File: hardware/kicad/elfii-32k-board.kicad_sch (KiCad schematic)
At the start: 14 parts, among them J1 ELFII_P3_86, SW1 RAM_PAGE_ENABLE, U1 74HC573, U2 CY62256-70PC, U3 74LS151, U4 CD4011

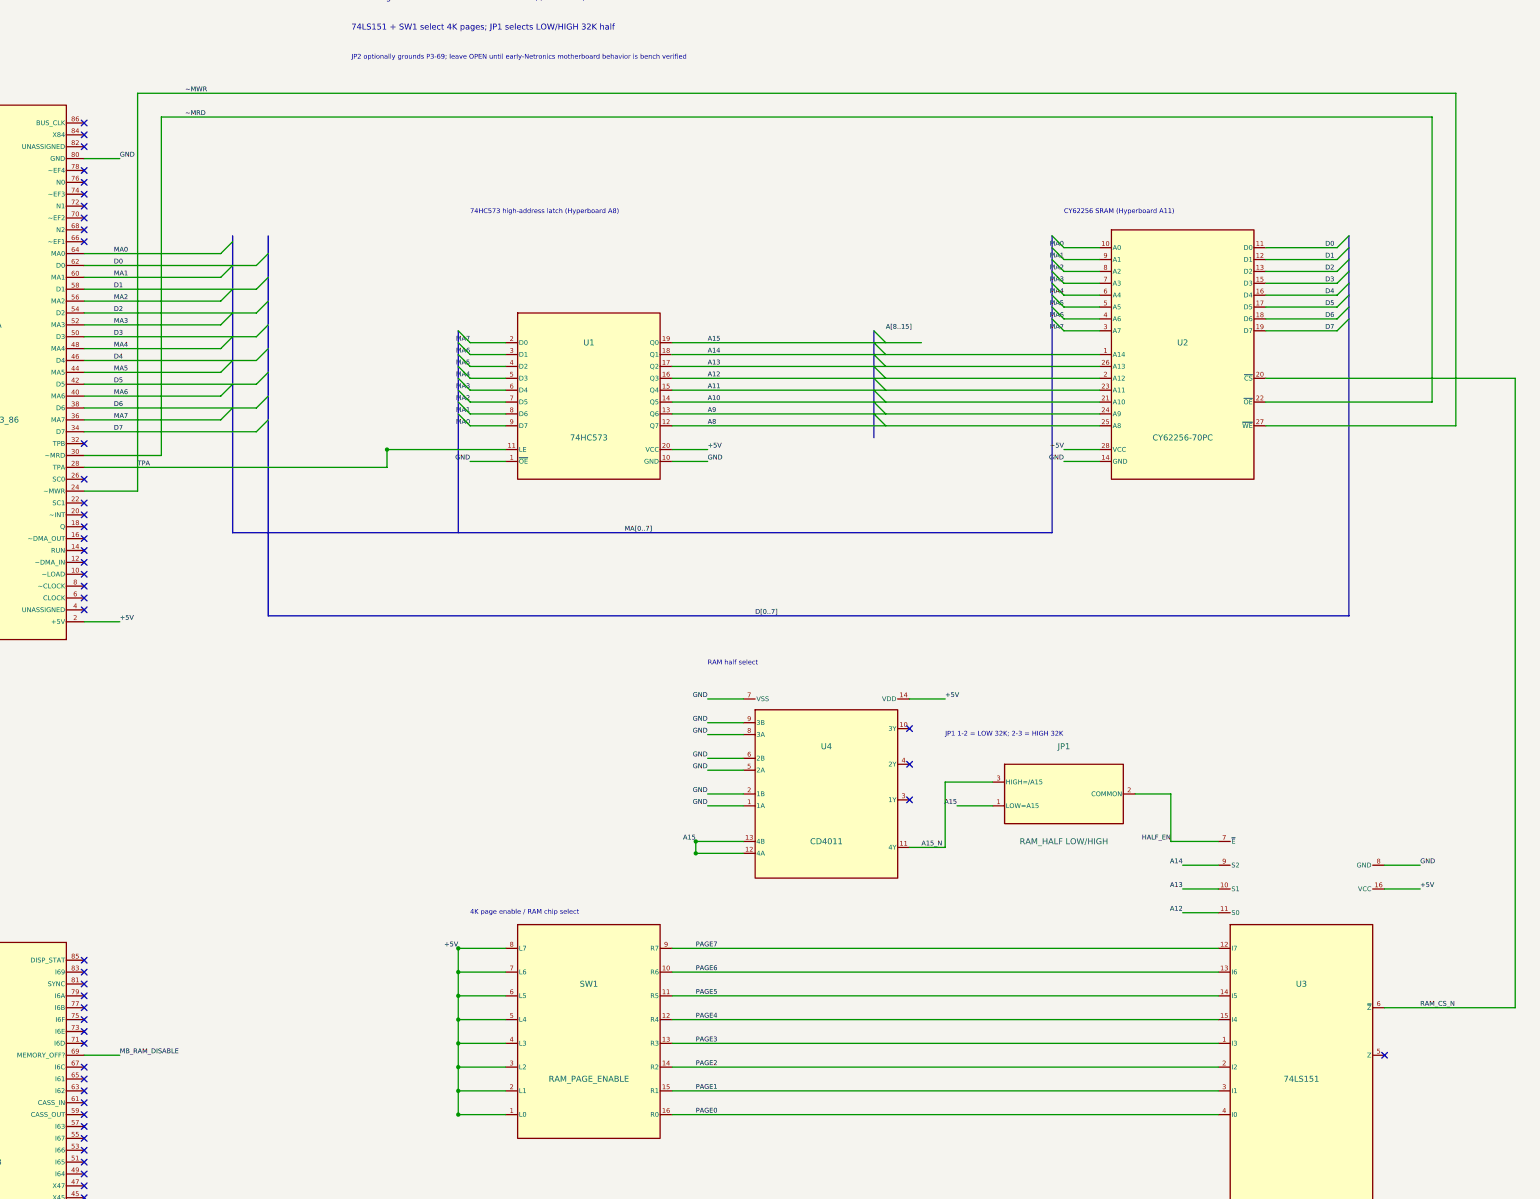
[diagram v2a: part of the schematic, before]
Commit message: Remove shorting bus entries, repair DIP supply rail, and isolate MWR
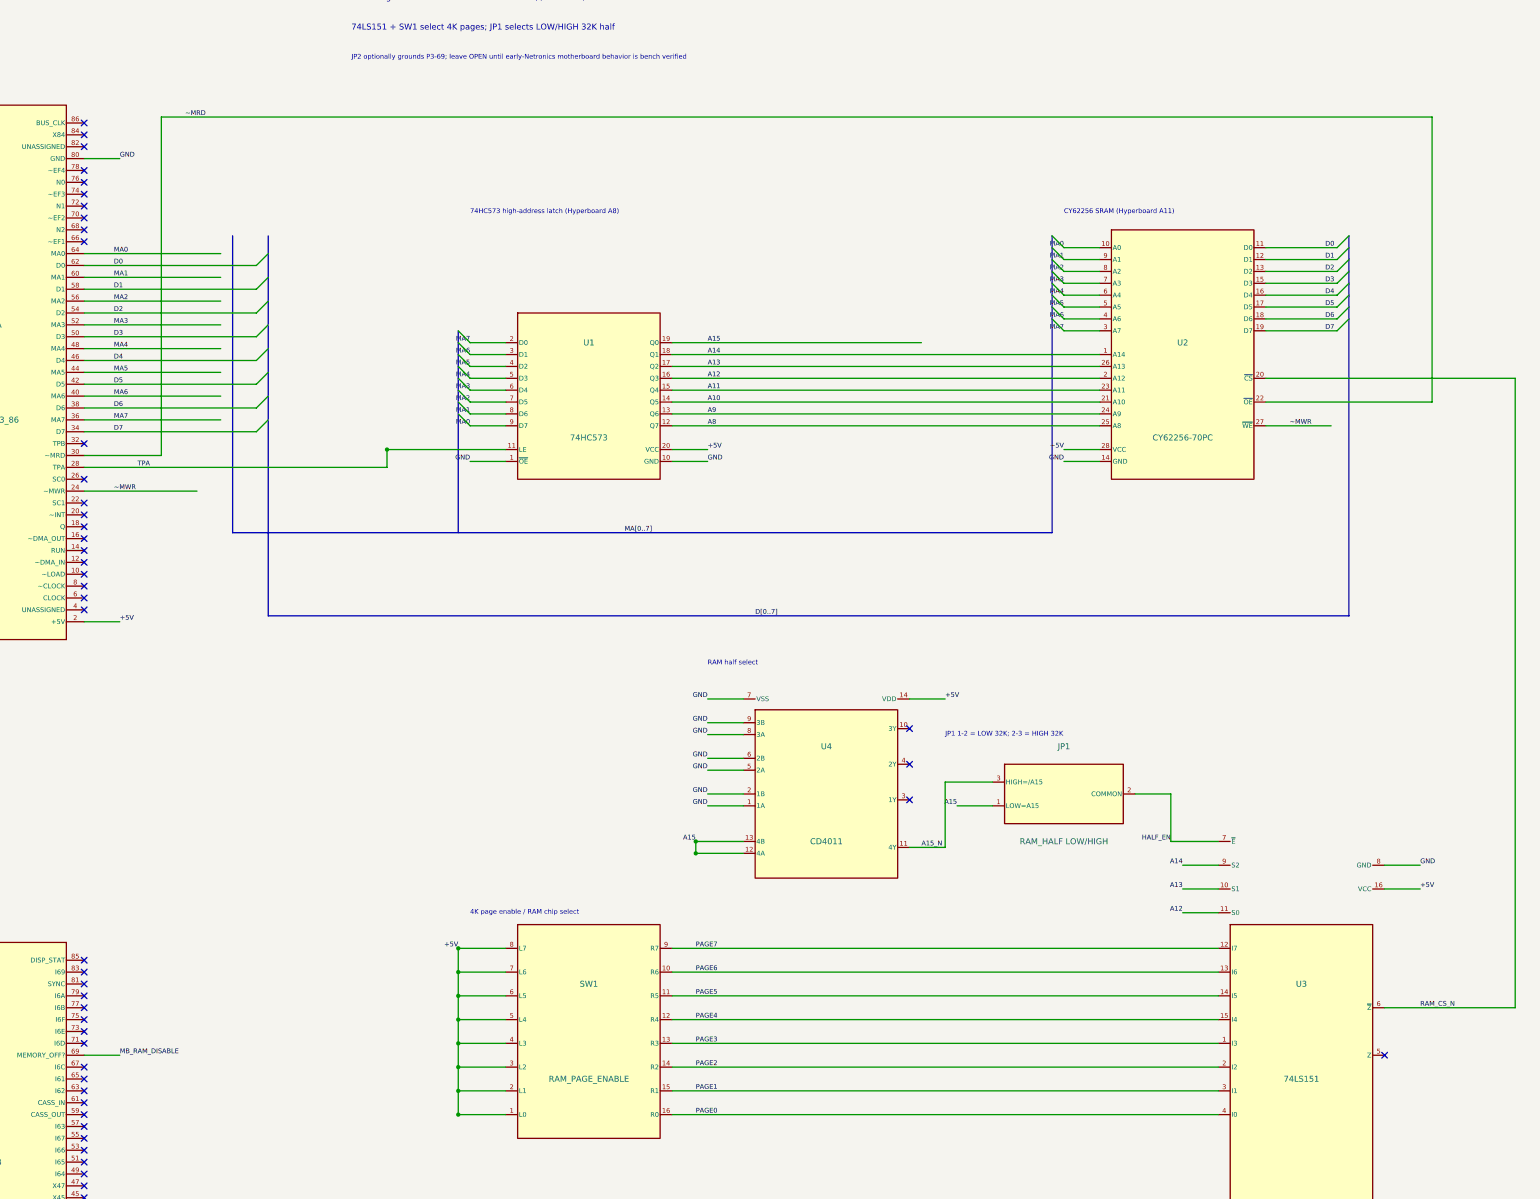
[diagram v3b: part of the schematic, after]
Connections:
- net TPA: no longer J1.24 (~MWR), U2.27 (~{WE})
- new net ~MWR: J1.24 (~MWR), U2.27 (~{WE})
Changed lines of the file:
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@@
 (generator "eeschema")
 (paper "A2")
-(title_block (title "Netronics ELF II 32K Static RAM Expansion") (date "2026-10-12") (rev "B1 - Hyperboard-derived schematic rebuild") (company "Community restoration project") (comment 1 "Historical bus interface; NOT validated/fabrication-ready"))
+(title_block (title "Netronics ELF II 32K Static RAM Expansion") (date "2026-10-12") (rev "B2 - electrical shorts cleanup") (company "Community restoration project") (comment 1 "Historical bus interface; NOT validated/fabrication-ready"))
 (symbol (lib_id "ELFII_Expansion:ELFII_P3") (at 76.2 113.03 180) (unit 1) (in_bom no) (on_board yes) (dnp no)
 (property "Reference" "J1" (at 76.2 102.87 0) (effects (font (size 1.27 1.27))))
@@
 (bus (pts (xy 302.26 83.82) (xy 302.26 147.32)) (stroke (width 0) (type default)))
 (label "MA[0..7]" (at 210.82 147.32 0) (effects (font (size 1.016 1.016)) (justify left bottom)))
-(bus_entry (at 127 85.09) (size -2.54 2.54) (stroke (width 0) (type default)))
 (wire (pts (xy 95.25 87.63) (xy 124.46 87.63)) (stroke (width 0) (type default)))
 (label "MA0" (at 101.6 87.63 0) (effects (font (size 1.016 1.016)) (justify left bottom)))
-(bus_entry (at 127 90.17) (size -2.54 2.54) (stroke (width 0) (type default)))
 (wire (pts (xy 95.25 92.71) (xy 124.46 92.71)) (stroke (width 0) (type default)))
 (label "MA1" (at 101.6 92.71 0) (effects (font (size 1.016 1.016)) (justify left bottom)))
-(bus_entry (at 127 95.25) (size -2.54 2.54) (stroke (width 0) (type default)))
 (wire (pts (xy 95.25 97.79) (xy 124.46 97.79)) (stroke (width 0) (type default)))
 (label "MA2" (at 101.6 97.79 0) (effects (font (size 1.016 1.016)) (justify left bottom)))
-(bus_entry (at 127 100.33) (size -2.54 2.54) (stroke (width 0) (type default)))
 (wire (pts (xy 95.25 102.87) (xy 124.46 102.87)) (stroke (width 0) (type default)))
 (label "MA3" (at 101.6 102.87 0) (effects (font (size 1.016 1.016)) (justify left bottom)))
-(bus_entry (at 127 105.41) (size -2.54 2.54) (stroke (width 0) (type default)))
 (wire (pts (xy 95.25 107.95) (xy 124.46 107.95)) (stroke (width 0) (type default)))
 (label "MA4" (at 101.6 107.95 0) (effects (font (size 1.016 1.016)) (justify left bottom)))
-(bus_entry (at 127 110.49) (size -2.54 2.54) (stroke (width 0) (type default)))
 (wire (pts (xy 95.25 113.03) (xy 124.46 113.03)) (stroke (width 0) (type default)))
 (label "MA5" (at 101.6 113.03 0) (effects (font (size 1.016 1.016)) (justify left bottom)))
-(bus_entry (at 127 115.57) (size -2.54 2.54) (stroke (width 0) (type default)))
 (wire (pts (xy 95.25 118.11) (xy 124.46 118.11)) (stroke (width 0) (type default)))
 (label "MA6" (at 101.6 118.11 0) (effects (font (size 1.016 1.016)) (justify left bottom)))
-(bus_entry (at 127 120.65) (size -2.54 2.54) (stroke (width 0) (type default)))
 (wire (pts (xy 95.25 123.19) (xy 124.46 123.19)) (stroke (width 0) (type default)))
 (label "MA7" (at 101.6 123.19 0) (effects (font (size 1.016 1.016)) (justify left bottom)))
@@
 (wire (pts (xy 347.98 104.14) (xy 363.22 104.14)) (stroke (width 0) (type default)))
 (label "D7" (at 360.68 104.14 0) (effects (font (size 1.016 1.016)) (justify left bottom)))
-(bus (pts (xy 264.16 104.14) (xy 264.16 127)) (stroke (width 0) (type default)))
-(label "A[8..15]" (at 266.7 104.14 0) (effects (font (size 1.016 1.016)) (justify left bottom)))
 (wire (pts (xy 220.98 109.22) (xy 312.42 109.22)) (stroke (width 0) (type default)))
 (label "A14" (at 228.6 109.22 0) (effects (font (size 1.016 1.016)) (justify left bottom)))
-(bus_entry (at 264.16 106.68) (size 2.54 2.54) (stroke (width 0) (type default)))
 (wire (pts (xy 220.98 111.76) (xy 312.42 111.76)) (stroke (width 0) (type default)))
 (label "A13" (at 228.6 111.76 0) (effects (font (size 1.016 1.016)) (justify left bottom)))
-(bus_entry (at 264.16 109.22) (size 2.54 2.54) (stroke (width 0) (type default)))
 (wire (pts (xy 220.98 114.3) (xy 312.42 114.3)) (stroke (width 0) (type default)))
 (label "A12" (at 228.6 114.3 0) (effects (font (size 1.016 1.016)) (justify left bottom)))
-(bus_entry (at 264.16 111.76) (size 2.54 2.54) (stroke (width 0) (type default)))
 (wire (pts (xy 220.98 116.84) (xy 312.42 116.84)) (stroke (width 0) (type default)))
 (label "A11" (at 228.6 116.84 0) (effects (font (size 1.016 1.016)) (justify left bottom)))
-(bus_entry (at 264.16 114.3) (size 2.54 2.54) (stroke (width 0) (type default)))
 (wire (pts (xy 220.98 119.38) (xy 312.42 119.38)) (stroke (width 0) (type default)))
 (label "A10" (at 228.6 119.38 0) (effects (font (size 1.016 1.016)) (justify left bottom)))
-(bus_entry (at 264.16 116.84) (size 2.54 2.54) (stroke (width 0) (type default)))
 (wire (pts (xy 220.98 121.92) (xy 312.42 121.92)) (stroke (width 0) (type default)))
 (label "A9" (at 228.6 121.92 0) (effects (font (size 1.016 1.016)) (justify left bottom)))
-(bus_entry (at 264.16 119.38) (size 2.54 2.54) (stroke (width 0) (type default)))
 (wire (pts (xy 220.98 124.46) (xy 312.42 124.46)) (stroke (width 0) (type default)))
 (label "A8" (at 228.6 124.46 0) (effects (font (size 1.016 1.016)) (justify left bottom)))
-(bus_entry (at 264.16 121.92) (size 2.54 2.54) (stroke (width 0) (type default)))
 (wire (pts (xy 220.98 106.68) (xy 274.32 106.68)) (stroke (width 0) (type default)))
 (label "A15" (at 228.6 106.68 0) (effects (font (size 1.016 1.016)) (justify left bottom)))
-(bus_entry (at 264.16 104.14) (size 2.54 2.54) (stroke (width 0) (type default)))
 (wire (pts (xy 95.25 133.35) (xy 160.02 133.35)) (stroke (width 0) (type default)))
 (wire (pts (xy 160.02 133.35) (xy 160.02 129.54)) (stroke (width 0) (type default)))
@@
 (wire (pts (xy 383.54 119.38) (xy 347.98 119.38)) (stroke (width 0) (type default)))
 (label "~MRD" (at 116.84 58.42 0) (effects (font (size 1.016 1.016)) (justify left bottom)))
-(wire (pts (xy 95.25 138.43) (xy 106.68 138.43)) (stroke (width 0) (type default)))
-(wire (pts (xy 106.68 138.43) (xy 106.68 53.34)) (stroke (width 0) (type default)))
-(wire (pts (xy 106.68 53.34) (xy 388.62 53.34)) (stroke (width 0) (type default)))
-(wire (pts (xy 388.62 53.34) (xy 388.62 124.46)) (stroke (width 0) (type default)))
-(wire (pts (xy 388.62 124.46) (xy 347.98 124.46)) (stroke (width 0) (type default)))
-(label "~MWR" (at 116.84 53.34 0) (effects (font (size 1.016 1.016)) (justify left bottom)))
 (wire (pts (xy 312.42 129.54) (xy 304.8 129.54)) (stroke (width 0) (type default)))
 (label "+5V" (at 304.8 129.54 0) (effects (font (size 1.016 1.016)) (justify right bottom)))
@@
 (wire (pts (xy 220.98 236.22) (xy 337.82 236.22)) (stroke (width 0) (type default)))
 (label "PAGE7" (at 226.06 236.22 0) (effects (font (size 1.016 1.016)) (justify left bottom)))
-(wire (pts (xy 175.26 236.22) (xy 175.26 271.78)) (stroke (width 0) (type default)))
+(wire (pts (xy 175.26 236.22) (xy 175.26 241.3)) (stroke (width 0) (type default)))
+(wire (pts (xy 175.26 241.3) (xy 175.26 246.38)) (stroke (width 0) (type default)))
+(wire (pts (xy 175.26 246.38) (xy 175.26 251.46)) (stroke (width 0) (type default)))
+(wire (pts (xy 175.26 251.46) (xy 175.26 256.54)) (stroke (width 0) (type default)))
+(wire (pts (xy 175.26 256.54) (xy 175.26 261.62)) (stroke (width 0) (type default)))
+(wire (pts (xy 175.26 261.62) (xy 175.26 266.7)) (stroke (width 0) (type default)))
+(wire (pts (xy 175.26 266.7) (xy 175.26 271.78)) (stroke (width 0) (type default)))
 (label "+5V" (at 175.26 236.22 0) (effects (font (size 1.016 1.016)) (justify right bottom)))
 (wire (pts (xy 175.26 271.78) (xy 185.42 271.78)) (stroke (width 0) (type default)))
@@
 (no_connect (at 95.25 241.3))
 (no_connect (at 95.25 238.76))
+(wire (pts (xy 95.25 138.43) (xy 119.38 138.43)) (stroke (width 0) (type default)))
+(label "~MWR" (at 101.6 138.43 0) (effects (font (size 1.016 1.016)) (justify left bottom)))
+(wire (pts (xy 347.98 124.46) (xy 361.95 124.46)) (stroke (width 0) (type default)))
+(label "~MWR" (at 353.06 124.46 0) (effects (font (size 1.016 1.016)) (justify left bottom)))
 (sheet_instances (path "/" (page "1")))
 )

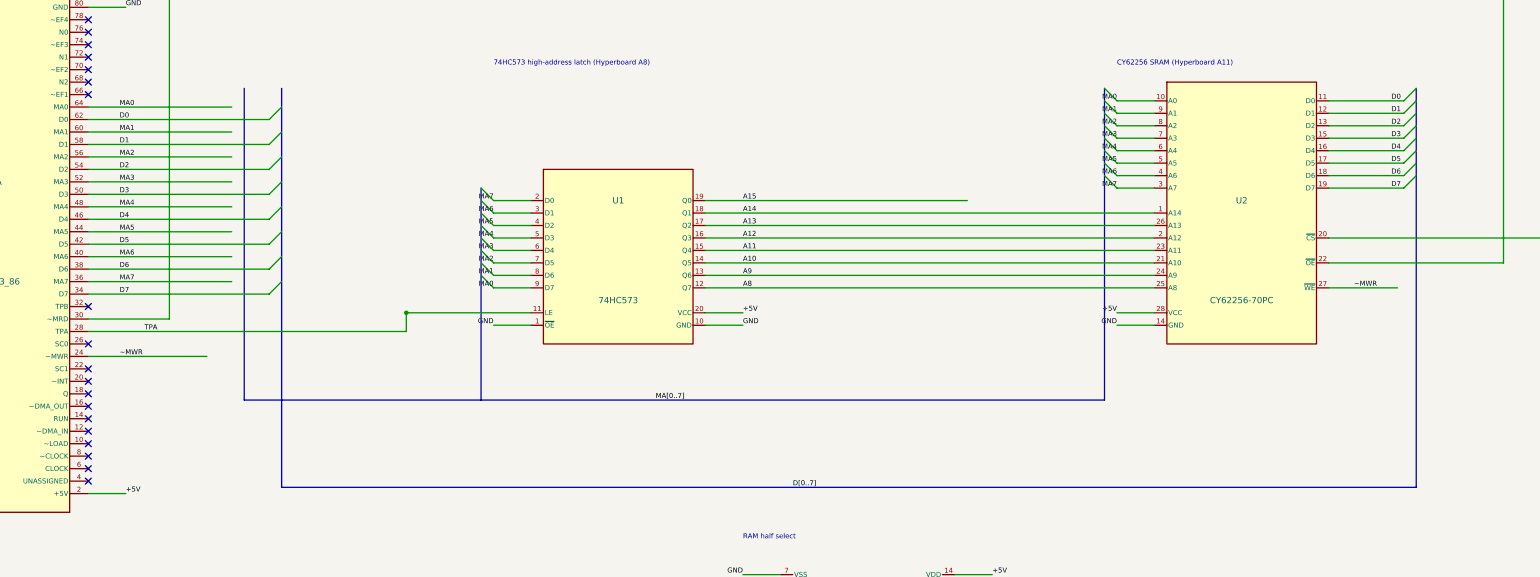
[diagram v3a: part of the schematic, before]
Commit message: Rebuild clean MA/D bus layout, trim connector stubs and correct DIP footprint
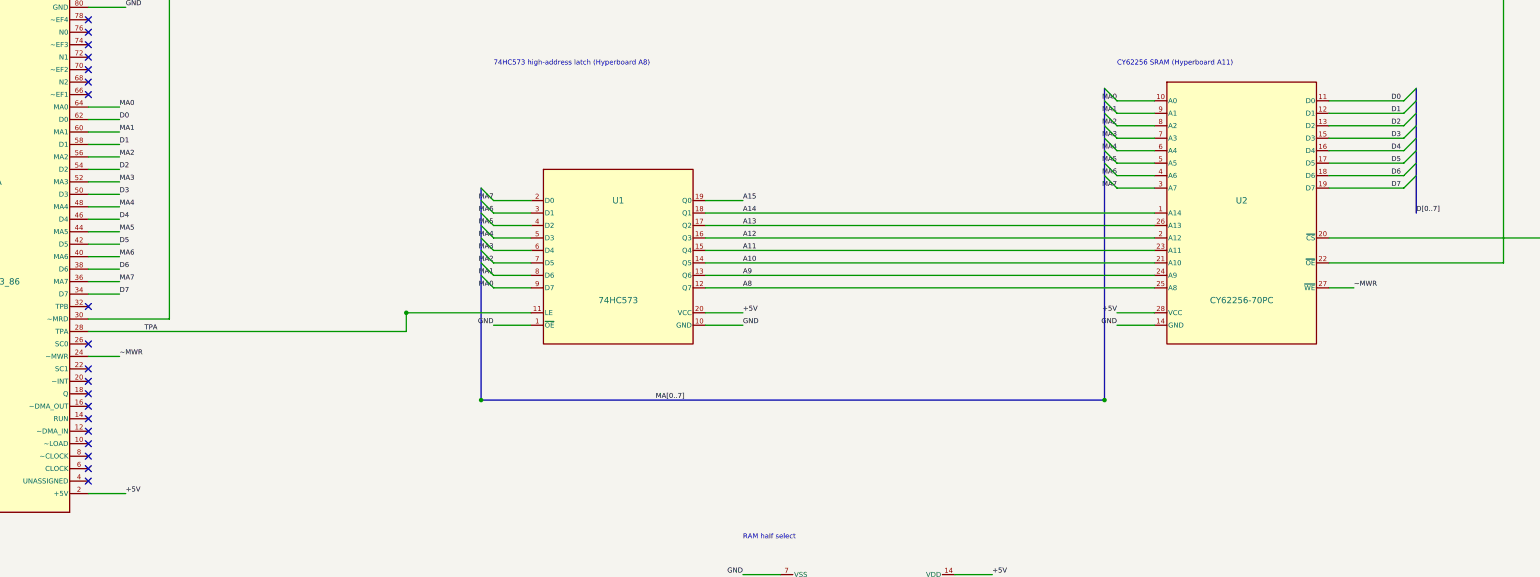
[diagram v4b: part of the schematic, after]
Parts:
- SW1: footprint Button_Switch_THT:SW_DIP_SPSTx08_Slide_9.78x21.8mm_W7.62mm_P2.54mm -> Button_Switch_THT:SW_DIP_SPSTx08_Slide_9.78x22.5mm_W7.62mm_P2.54mm

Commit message: Assign RN1 a valid SIP9 footprint in live KiCad schematic
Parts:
- RN1: footprint (none) -> Resistor_THT:R_Array_SIP9
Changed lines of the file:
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@@
 (property "Reference" "RN1" (at 254 325.11999999999995 0) (effects (font (size 1.27 1.27))))
 (property "Value" "8x22K PULLDOWN" (at 254 345.44 0) (effects (font (size 1.27 1.27))))
-(property "Footprint" "" (at 254 335.28 0) (effects (font (size 1.27 1.27)) hide))
+(property "Footprint" "Resistor_THT:R_Array_SIP9" (at 254 335.28 0) (effects (font (size 1.27 1.27)) hide))
 (instances (project "elfii-32k-board" (path "/89d8d6a8-e087-4cc0-b51a-852515026bd4" (reference "RN1") (unit 1))))
 )
